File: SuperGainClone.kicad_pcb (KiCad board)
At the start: 2 copper layers, 99 x 116 mm, 99 parts, among them J1 Conn_01x02, J2 Conn_01x03, J3 Conn_01x02, J4 Conn_01x02, J5 Conn_01x02, Q1 TIP41C, Q2 TIP42C, U1 OPA2604A, U2 LM3886T, U3 OPA2604A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

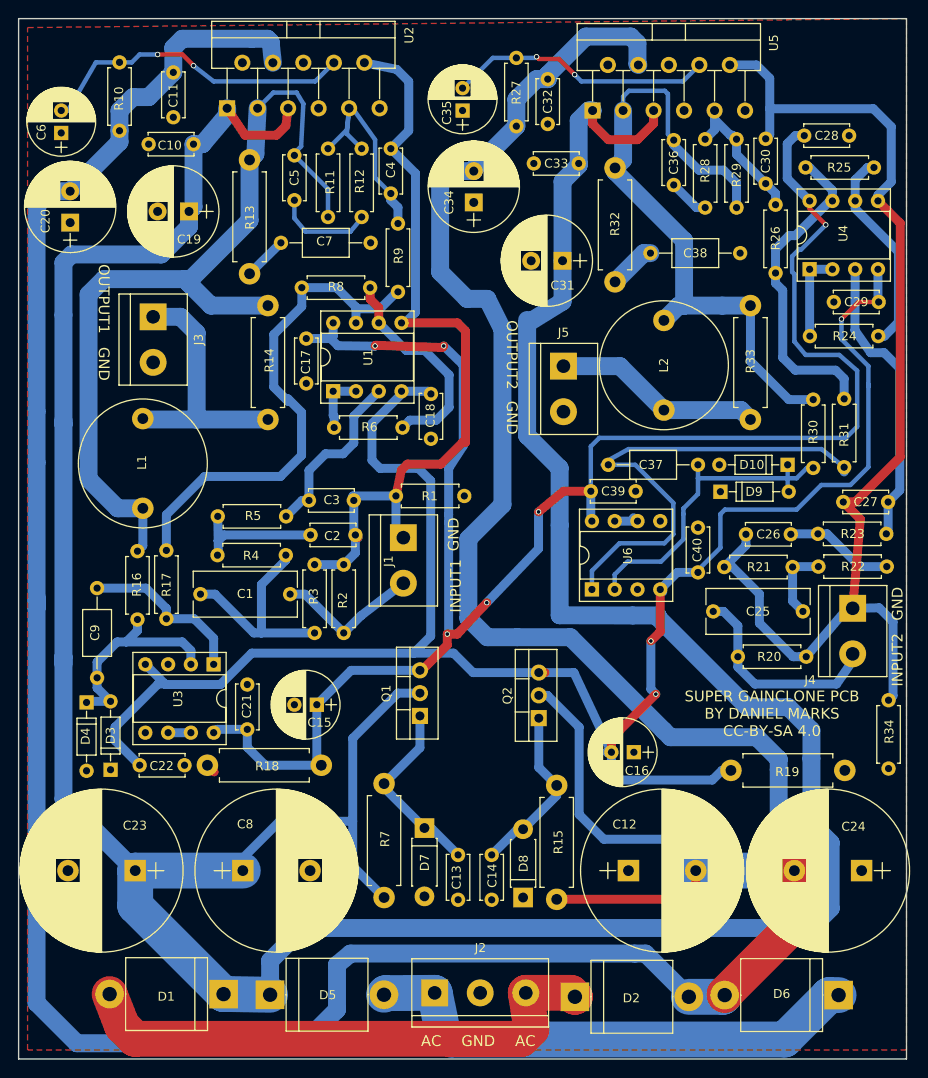
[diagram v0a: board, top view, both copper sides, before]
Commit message: Rearranged some components
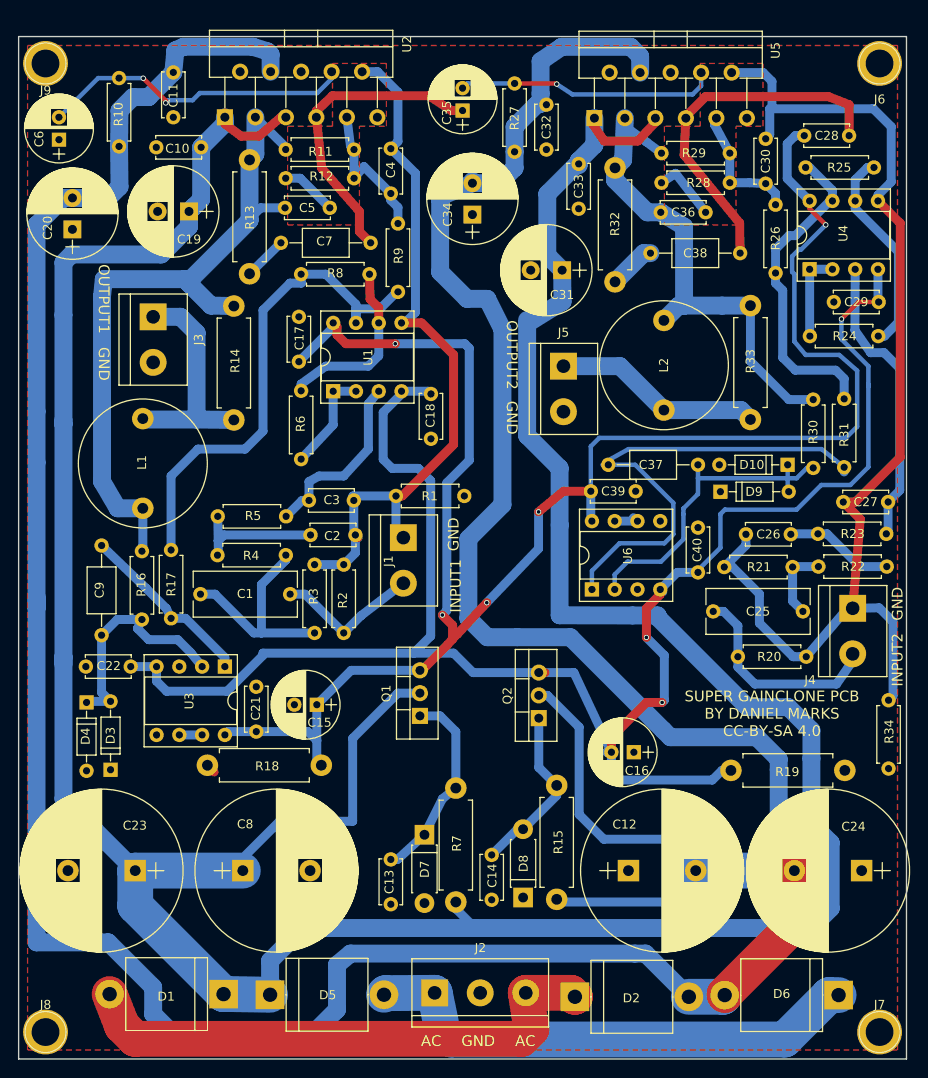
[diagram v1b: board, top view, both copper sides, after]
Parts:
- added J6: Conn_01x01, Connectors:1pin, F.Cu at (121.0, 52.0)
- added J7: Conn_01x01, Connectors:1pin, F.Cu at (121.0, 160.0)
- added J8: Conn_01x01, Connectors:1pin, F.Cu at (28.0, 160.0)
- added J9: Conn_01x01, Connectors:1pin, F.Cu at (28.0, 52.0)
- moved R6 12.0 mm to (56.5, 88.5), turned to 270 degrees
- moved C22 11.0 mm to (37.5, 119.2), turned to 180 degrees
- moved R7 8.02 mm to (73.8, 145.5)
- moved C13 7.52 mm to (66.5, 140.8)
- moved R28 5.58 mm to (104.3, 65.3), turned to 180 degrees
- moved C9 4.78 mm to (34.2, 115.8)
- moved C36 4.68 mm to (101.6, 68.6), turned to 180 degrees
- moved C5 4.04 mm to (59.7, 68.1), turned to 180 degrees
- moved R14 3.80 mm to (49.0, 91.8)
- moved R12 3.41 mm to (62.4, 64.8), turned to 180 degrees
- moved R11 2.90 mm to (62.4, 61.6), turned to 180 degrees
- moved R27 2.86 mm to (80.3, 61.9)
- moved C32 2.85 mm to (83.8, 56.6)
- moved C17 2.70 mm to (56.2, 85.2), turned to 90 degrees
- moved R10 1.75 mm to (36.2, 61.2)
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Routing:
- net GND: track 1.20 -> 75.7 mm
- net Net-(C5-Pad2): track 99.9 -> 82.3 mm
- net Net-(C36-Pad2): track 75.0 -> 57.4 mm
- net +24V: track 390.9 -> 381.6 mm
- net -15V: track 210.7 -> 201.4 mm
- net Net-(C4-Pad1): track 25.8 -> 17.1 mm
- net GNDS: track 91.5 -> 84.0 mm
- net Net-(R6-Pad2): track 6.63 -> 11.5 mm
- net Net-(C5-Pad1): track 11.0 -> 6.29 mm
- net Net-(R6-Pad1): track 24.5 -> 20.2 mm
- net Net-(J3-Pad1): track 29.2 -> 25.4 mm
- net Net-(C36-Pad1): track 4.54 -> 7.38 mm
- net Net-(C30-Pad1): track 17.1 -> 14.5 mm
- net Net-(C9-Pad1): track 24.1 -> 25.9 mm
- net Net-(C13-Pad1): track 21.0 -> 22.2 mm
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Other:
- board size 99 x 116 mm -> 99 x 114 mm

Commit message: Fixed DC servo feedback
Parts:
- C12, C23, C24, C8: value 20000 uF -> 4700 uF
- U1, U4: value OPA2604A -> LM4562/TL072
- U3, U6: value OPA2604A -> TL072
- moved C30 10.0 mm to (111.8, 56.0)
- moved C28 8.68 mm to (109.2, 68.0), turned to 90 degrees
- moved R1 8.51 mm to (75.5, 99.0), turned to 180 degrees
- moved R26 7.81 mm to (113.3, 61.0), turned to 0 degrees
- moved R25 0.93 mm to (113.5, 64.1)
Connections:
- R31 pad 1: Net-(R25-Pad1) -> Net-(R24-Pad1)
- R6 pad 1: Net-(R6-Pad1) -> Net-(R17-Pad1)
- R8 pad 1: Net-(R17-Pad1) -> Net-(R8-Pad1)
- R8 pad 2: Net-(R6-Pad1) -> Net-(R17-Pad1)
- R9 pad 2: Net-(R17-Pad1) -> Net-(R8-Pad1)
- U1 pad 6: Net-(R6-Pad1) -> Net-(R17-Pad1)
- U1 pad 7: Net-(R17-Pad1) -> Net-(R8-Pad1)
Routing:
- net Net-(R24-Pad1): track 23.4 -> 56.3 mm
- net Net-(R25-Pad1): track 36.4 -> 13.3 mm
- net Net-(R6-Pad1): track 20.2 -> 0.00 mm
- net Net-(R8-Pad1): track 0.00 -> 16.6 mm
- net Net-(C30-Pad1): track 14.5 -> 28.3 mm
- net Net-(R17-Pad1): track 57.2 -> 44.7 mm
- net +15V: track 199.2 -> 191.6 mm
- net GNDS: track 84.0 -> 90.2 mm
- net GND: track 75.7 -> 79.4 mm
- net GNDS2: track 128.0 -> 125.2 mm
- net Net-(C37-Pad1): track 36.4 -> 39.0 mm
- net -15V: track 201.4 -> 199.0 mm
- net Net-(C36-Pad1): track 7.38 -> 6.03 mm
- net -24V: track 438.5 -> 439.4 mm
- net Net-(C9-Pad1): track 25.9 -> 25.1 mm
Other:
- board text added: "1"
- board text added: "LM4562"
- board text added: "TIP41C"
- board text added: "TIP42C"
